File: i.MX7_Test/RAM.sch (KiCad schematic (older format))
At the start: 3 parts, among them U2 MCIMX7D7DVM10SC

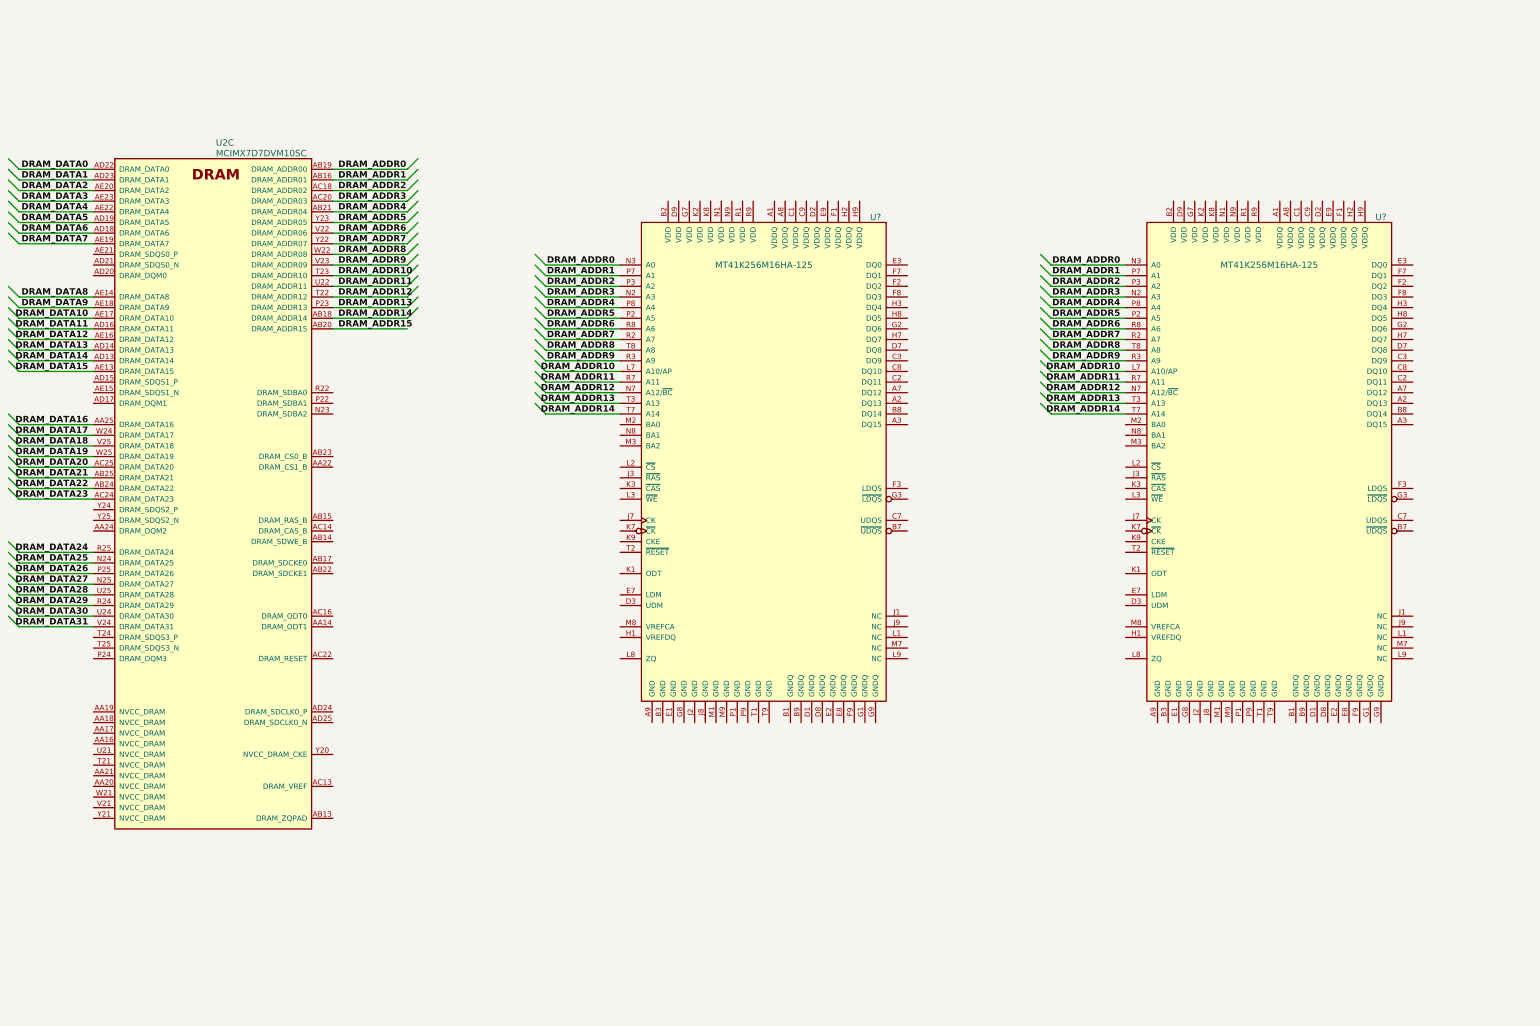
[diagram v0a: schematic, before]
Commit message: finished DDR3L RAM for 1GB with 2 banks
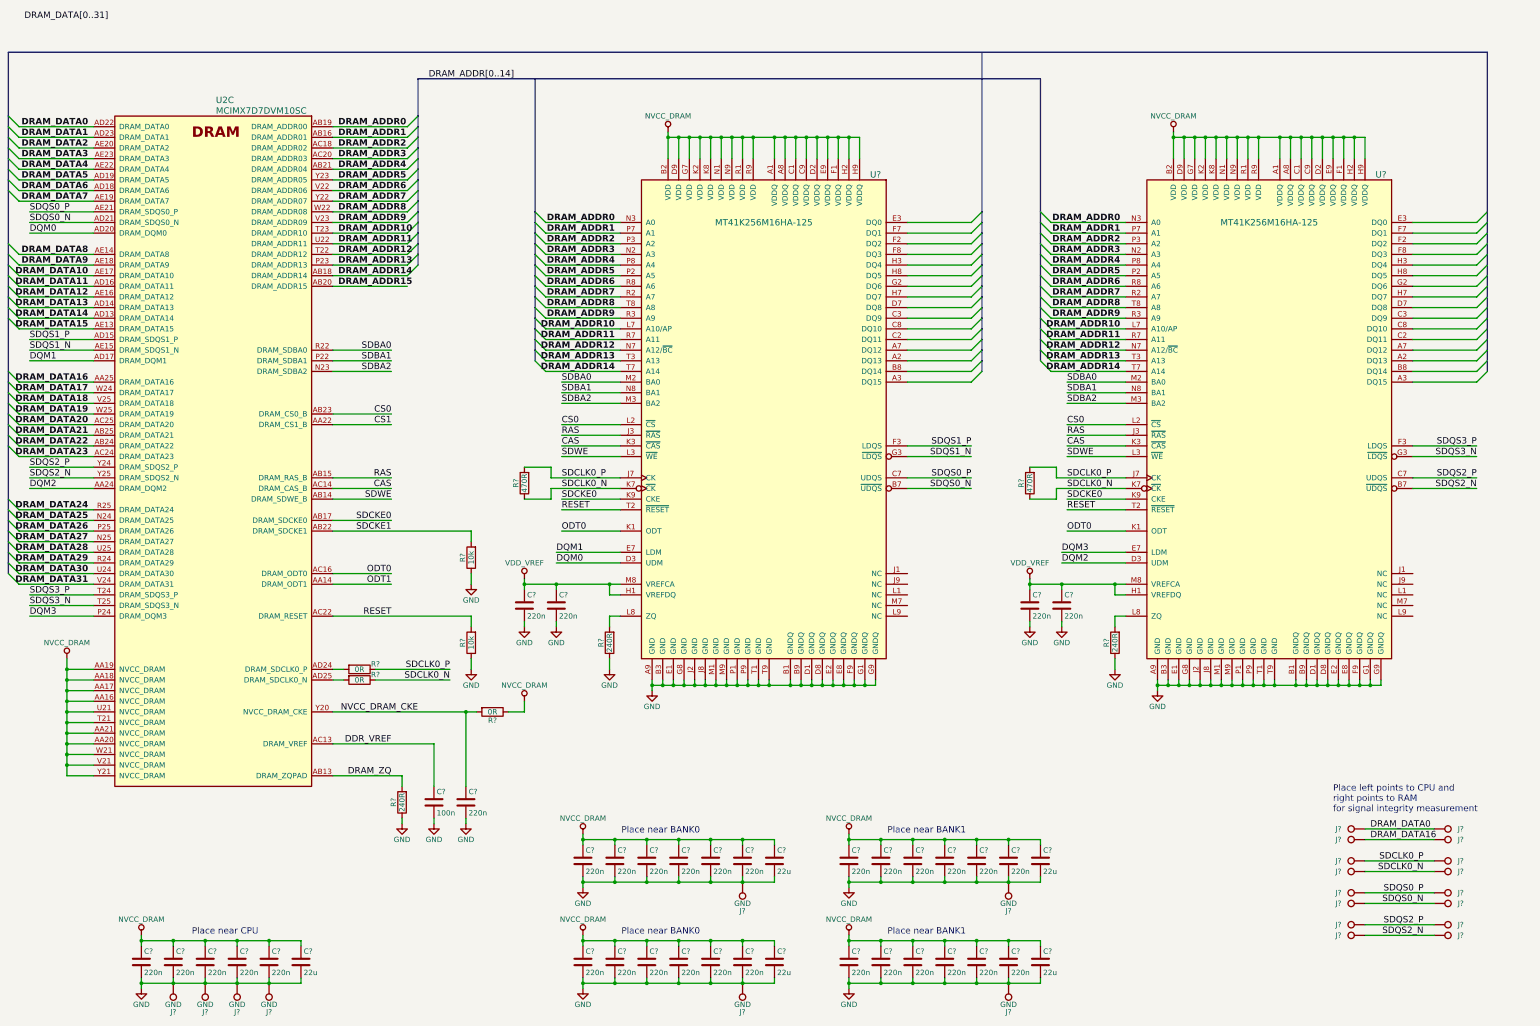
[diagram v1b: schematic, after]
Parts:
- added C?: 100n, symbol C
- added C? (x34): 220n, symbol C
- added C? (x5): 22u, symbol C
- added J? (x24): GND, symbol TEST_1P
- added R? (x3): 0R, symbol R
- added R? (x3): 240R, symbol R
- added R? (x2): 10k, symbol R
- added R? (x2): 470R, symbol R
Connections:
- net DRAM_DATA0: now also J?.1, J?.1
- net DRAM_DATA16: now also J?.1, J?.1
- net ODT1: now reaches U2.AA14 (DRAM_ODT1)
- net NVCC_DRAM: now reaches U2.AA16 (NVCC_DRAM)
- net NVCC_DRAM: now also U2.AA17 (NVCC_DRAM), U2.AA18 (NVCC_DRAM), U2.AA19 (NVCC_DRAM), U2.AA20 (NVCC_DRAM), U2.AA21 (NVCC_DRAM), U2.T21 (NVCC_DRAM), U2.U21 (NVCC_DRAM), U2.V21 (NVCC_DRAM), U2.W21 (NVCC_DRAM), U2.Y21 (NVCC_DRAM), U?.A1 (VDDQ), U?.A1 (VDDQ), U?.A8 (VDDQ), U?.A8 (VDDQ), U?.B2 (VDD), U?.B2 (VDD), U?.C1 (VDDQ), U?.C1 (VDDQ), U?.C9 (VDDQ), U?.C9 (VDDQ), U?.D2 (VDDQ), U?.D2 (VDDQ), U?.D9 (VDD), U?.D9 (VDD), U?.E9 (VDDQ), U?.E9 (VDDQ), U?.F1 (VDDQ), U?.F1 (VDDQ), U?.G7 (VDD), U?.G7 (VDD), U?.H2 (VDDQ), U?.H2 (VDDQ), U?.H9 (VDDQ), U?.H9 (VDDQ), U?.K2 (VDD), U?.K2 (VDD), U?.K8 (VDD), U?.K8 (VDD), U?.N1 (VDD), U?.N1 (VDD), U?.N9 (VDD), U?.N9 (VDD), U?.R1 (VDD), U?.R1 (VDD), U?.R9 (VDD), U?.R9 (VDD), C?.1, C?.1, C?.1, C?.1, C?.1, C?.1, C?.1, C?.1, C?.1, C?.1, C?.1, C?.1, C?.1, C?.1, C?.1, C?.1, C?.1, C?.1, C?.1, C?.1, C?.1, C?.1, C?.1, C?.1, C?.1, C?.1, C?.1, C?.1, C?.1, C?.1, C?.1, C?.1, C?.1, C?.1, R?.1
- net CS1: now reaches U2.AA22 (DRAM_CS1_B)
- net DQM2: now reaches U2.AA24 (DRAM_DQM2)
- net DQM2: now also U?.D3 (UDM)
- net DRAM_ZQ: now reaches U2.AB13 (DRAM_ZQPAD)
- net DRAM_ZQ: now also R?.2
- net SDWE: now reaches U2.AB14 (DRAM_SDWE_B)
- net SDWE: now also U?.L3 (~WE), U?.L3 (~WE)
- net RAS: now reaches U2.AB15 (DRAM_RAS_B)
- net RAS: now also U?.J3 (~RAS), U?.J3 (~RAS)
- net SDCKE0: now reaches U2.AB17 (DRAM_SDCKE0)
- net SDCKE0: now also U?.K9 (CKE), U?.K9 (CKE)
- net SDCKE1: now reaches U2.AB22 (DRAM_SDCKE1)
- net SDCKE1: now also R?.2
- net CS0: now reaches U2.AB23 (DRAM_CS0_B)
- net CS0: now also U?.L2 (~CS), U?.L2 (~CS)
- net DDR_VREF: now reaches U2.AC13 (DRAM_VREF)
- net DDR_VREF: now also C?.1
- net CAS: now reaches U2.AC14 (DRAM_CAS_B)
- net CAS: now also U?.K3 (~CAS), U?.K3 (~CAS)
- net ODT0: now reaches U2.AC16 (DRAM_ODT0)
- net ODT0: now also U?.K1 (ODT), U?.K1 (ODT)
- net RESET: now reaches U2.AC22 (DRAM_RESET)
- net RESET: now also U?.T2 (~RESET), U?.T2 (~RESET), R?.2
- net SDQS1_P: now reaches U2.AD15 (DRAM_SDQS1_P)
- net SDQS1_P: now also U?.F3 (LDQS)
- net DQM1: now reaches U2.AD17 (DRAM_DQM1)
- net DQM1: now also U?.E7 (LDM)
- net DQM0: now reaches U2.AD20 (DRAM_DQM0)
- net DQM0: now also U?.D3 (UDM)
- net SDQS0_N: now reaches U2.AD21 (DRAM_SDQS0_N)
- net SDQS0_N: now also U?.B7 (~UDQS), J?.1, J?.1
- net at U2.AD24 (DRAM_SDCLK0_P): now also R?.2
- net at U2.AD25 (DRAM_SDCLK0_N): now also R?.2
- net SDQS1_N: now reaches U2.AE15 (DRAM_SDQS1_N)
- net SDQS1_N: now also U?.G3 (~LDQS)
- net SDQS0_P: now reaches U2.AE21 (DRAM_SDQS0_P)
- net SDQS0_P: now also U?.C7 (UDQS), J?.1, J?.1
- net SDBA2: now reaches U2.N23 (DRAM_SDBA2)
- net SDBA2: now also U?.M3 (BA2), U?.M3 (BA2)
- net SDBA1: now reaches U2.P22 (DRAM_SDBA1)
- net SDBA1: now also U?.N8 (BA1), U?.N8 (BA1)
- net DQM3: now reaches U2.P24 (DRAM_DQM3)
- net DQM3: now also U?.E7 (LDM)
- net SDBA0: now reaches U2.R22 (DRAM_SDBA0)
- net SDBA0: now also U?.M2 (BA0), U?.M2 (BA0)
- net SDQS3_P: now reaches U2.T24 (DRAM_SDQS3_P)
- net SDQS3_P: now also U?.F3 (LDQS)
- net SDQS3_N: now reaches U2.T25 (DRAM_SDQS3_N)
- net SDQS3_N: now also U?.G3 (~LDQS)
- net NVCC_DRAM_CKE: now reaches U2.Y20 (NVCC_DRAM_CKE)
- net NVCC_DRAM_CKE: now also C?.1, R?.2
- net SDQS2_P: now reaches U2.Y24 (DRAM_SDQS2_P)
- net SDQS2_P: now also U?.C7 (UDQS), J?.1, J?.1
- net SDQS2_N: now reaches U2.Y25 (DRAM_SDQS2_N)
- net SDQS2_N: now also U?.B7 (~UDQS), J?.1, J?.1
- net GND: now reaches U?.A9 (GND)
- net GND: now also U?.A9 (GND), U?.B1 (GNDQ), U?.B1 (GNDQ), U?.B3 (GND), U?.B3 (GND), U?.B9 (GNDQ), U?.B9 (GNDQ), U?.D1 (GNDQ), U?.D1 (GNDQ), U?.D8 (GNDQ), U?.D8 (GNDQ), U?.E1 (GND), U?.E1 (GND), U?.E2 (GNDQ), U?.E2 (GNDQ), U?.E8 (GNDQ), U?.E8 (GNDQ), U?.F9 (GNDQ), U?.F9 (GNDQ), U?.G1 (GNDQ), U?.G1 (GNDQ), U?.G8 (GND), U?.G8 (GND), U?.G9 (GNDQ), U?.G9 (GNDQ), U?.J2 (GND), U?.J2 (GND), U?.J8 (GND), U?.J8 (GND), U?.M1 (GND), U?.M1 (GND), U?.M9 (GND), U?.M9 (GND), U?.P1 (GND), U?.P1 (GND), U?.P9 (GND), U?.P9 (GND), U?.T1 (GND), U?.T1 (GND), U?.T9 (GND), U?.T9 (GND), C?.2, C?.2, C?.2, C?.2, C?.2, C?.2, C?.2, C?.2, C?.2, C?.2, C?.2, C?.2, C?.2, C?.2, C?.2, C?.2, C?.2, C?.2, C?.2, C?.2, C?.2, C?.2, C?.2, C?.2, C?.2, C?.2, C?.2, C?.2, C?.2, C?.2, C?.2, C?.2, C?.2, C?.2, C?.2, C?.2, C?.2, C?.2, C?.2, C?.2, J?.1, J?.1, J?.1, J?.1, J?.1, J?.1, J?.1, J?.1, R?.1, R?.1, R?.1, R?.1, R?.1
- net VDD_VREF: now reaches U?.H1 (VREFDQ)
- net VDD_VREF: now also U?.H1 (VREFDQ), U?.M8 (VREFCA), U?.M8 (VREFCA), C?.1, C?.1, C?.1, C?.1
- net SDCLK0_P: now reaches U?.J7 (CK)
- net SDCLK0_P: now also U?.J7 (CK), J?.1, J?.1, R?.1, R?.2, R?.2
- net SDCLK0_N: now reaches U?.K7 (~CK)
- net SDCLK0_N: now also U?.K7 (~CK), J?.1, J?.1, R?.1, R?.1, R?.1
- net at U?.L8 (ZQ): now also R?.2 (x2)
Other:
- note added: "Place left points to CPU and \nright points to RAM\nfor signal integrity measurement"
- note added: "Place near BANK0"
- note added: "Place near BANK1"
- note added: "Place near CPU"
- moved on the sheet: U2C, U?

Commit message: Added some schematics for PMIC Added some Documentation for i.mx7
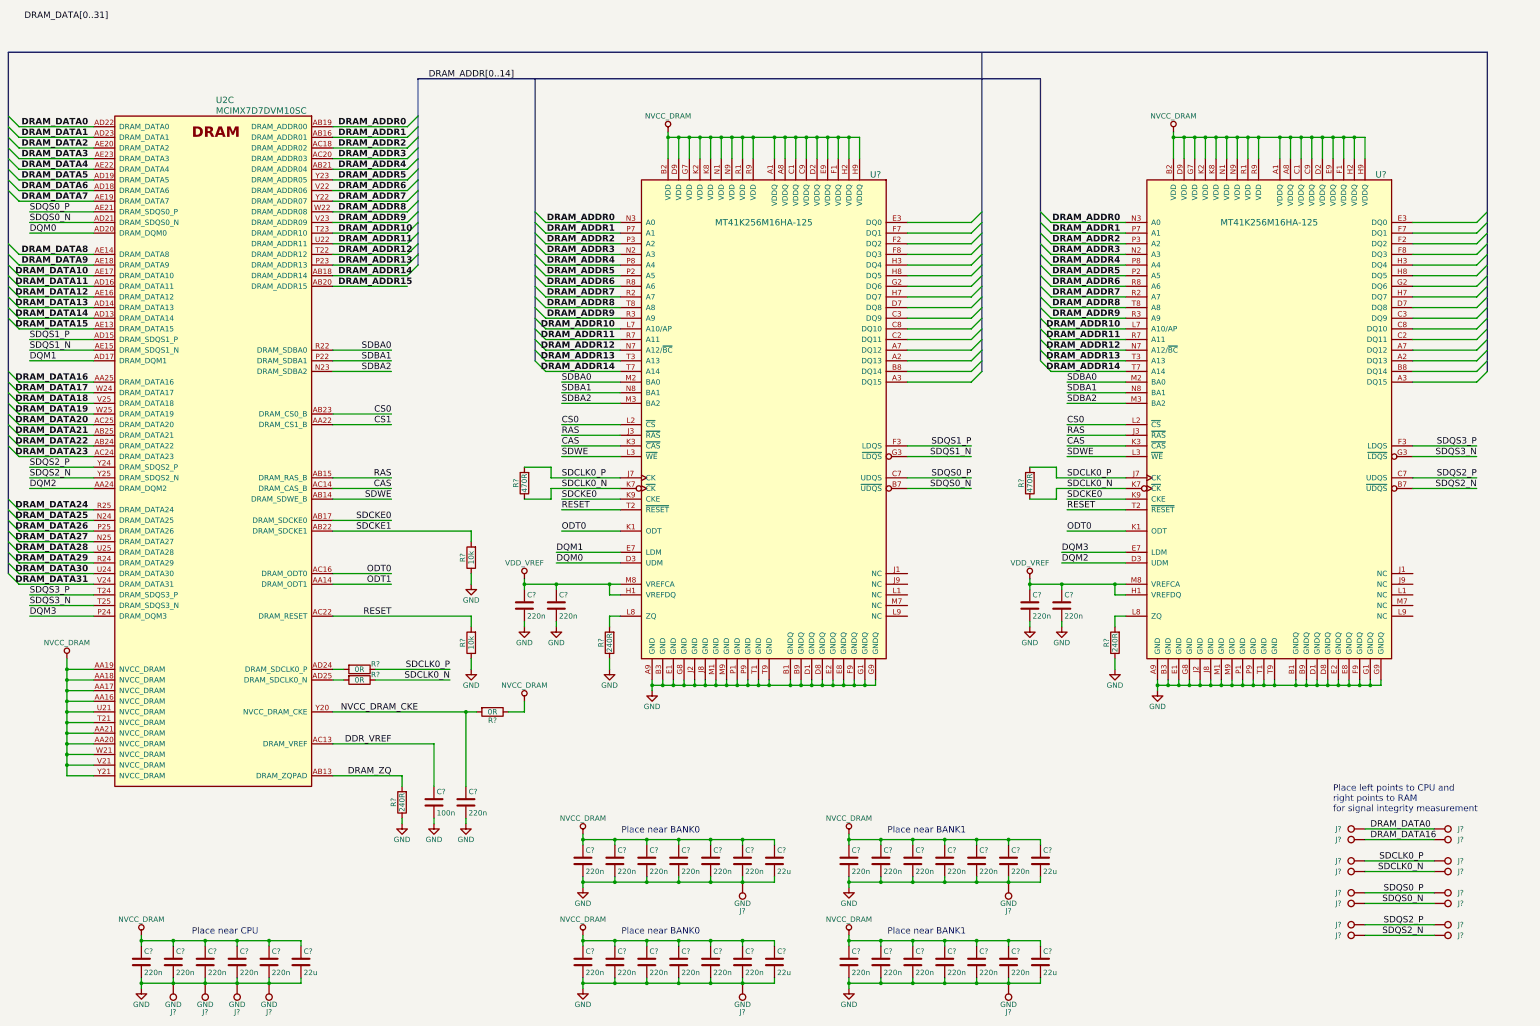
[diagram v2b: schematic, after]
